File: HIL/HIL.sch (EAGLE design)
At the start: 245 parts, among them J1 JTAG_ARM_10PIN, J4 JTAG_ARM_10PIN, U1 CD74HC4067SM96, U10 INA219AIDCNR, U11 INA219AIDCNR, U12 INA219AIDCNR, U14 ADUM1201ARZ, U15 SN65HVD230D, U16 TL1963AKTTR., U17 FT230XS, U2 TL1963AKTTR., U3 CD74HC4067SM96, U4 CD74HC4067SM96, U5 MCP4725A0T-E/CH, U6 TL1963AKTTR., U7 MCP2003-E/SN, U8 TM4C1294NCPDT, U9 INA219AIDCNR, X1 A1944-50, X2 A1944-50, X4 A1944-50, Y3 NX3225GA

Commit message: smal fixes
better 3v3 plane coverage
add labels
fix tracks which are not straight or 45 degree
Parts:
- renumbered STANDOFF1 to STANDOFF3, STANDOFF5 to STANDOFF4
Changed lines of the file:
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@@
 <part name="U$5" library="SparkFun-DiscreteSemi" deviceset="MMBZ27VCLT1" device="" value="zener_3.3V"/>
 <part name="U$10" library="SparkFun-DiscreteSemi" deviceset="MMBZ27VCLT1" device="" value="zener_3.3V"/>
-<part name="STANDOFF1" library="SparkFun-Electromechanical" deviceset="STAND-OFF" device=""/>
+<part name="STANDOFF3" library="SparkFun-Electromechanical" deviceset="STAND-OFF" device=""/>
 <part name="STANDOFF2" library="SparkFun-Electromechanical" deviceset="STAND-OFF" device=""/>
-<part name="STANDOFF5" library="SparkFun-Electromechanical" deviceset="STAND-OFF" device=""/>
+<part name="STANDOFF4" library="SparkFun-Electromechanical" deviceset="STAND-OFF" device=""/>
 <part name="STANDOFF6" library="SparkFun-Electromechanical" deviceset="STAND-OFF" device=""/>
 <part name="R72" library="resistor" deviceset="R-EU_" device="R0402" value="4k7"/>
@@
 <instance part="S1" gate="1" x="27.94" y="127" rot="R270"/>
 <instance part="F1" gate="1" x="22.86" y="152.4" rot="R270"/>
-<instance part="STANDOFF1" gate="G$1" x="289.56" y="27.94"/>
+<instance part="STANDOFF3" gate="G$1" x="289.56" y="27.94"/>
 <instance part="STANDOFF2" gate="G$1" x="294.64" y="27.94"/>
-<instance part="STANDOFF5" gate="G$1" x="309.88" y="27.94"/>
+<instance part="STANDOFF4" gate="G$1" x="309.88" y="27.94"/>
 <instance part="STANDOFF6" gate="G$1" x="314.96" y="27.94"/>
 <instance part="R72" gate="G$1" x="154.94" y="195.58" rot="R180"/>

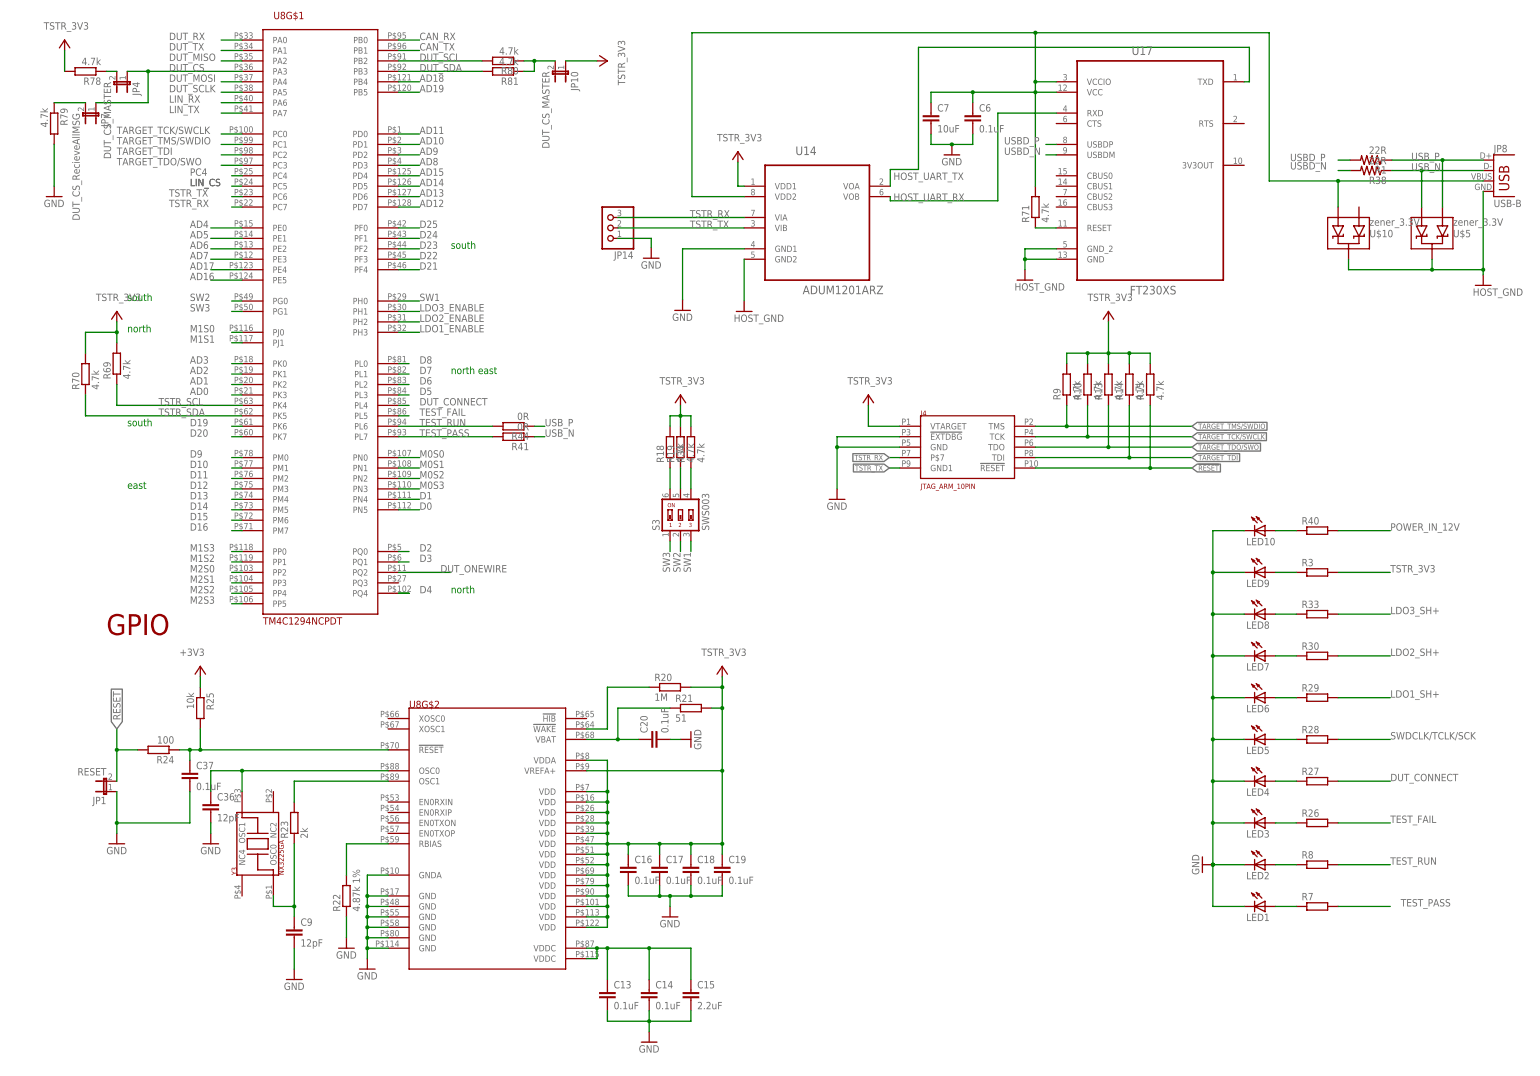
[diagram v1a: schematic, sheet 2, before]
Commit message: Change:  - MCU to a proper package Add:        - labels                 - i2c header                 - UART header
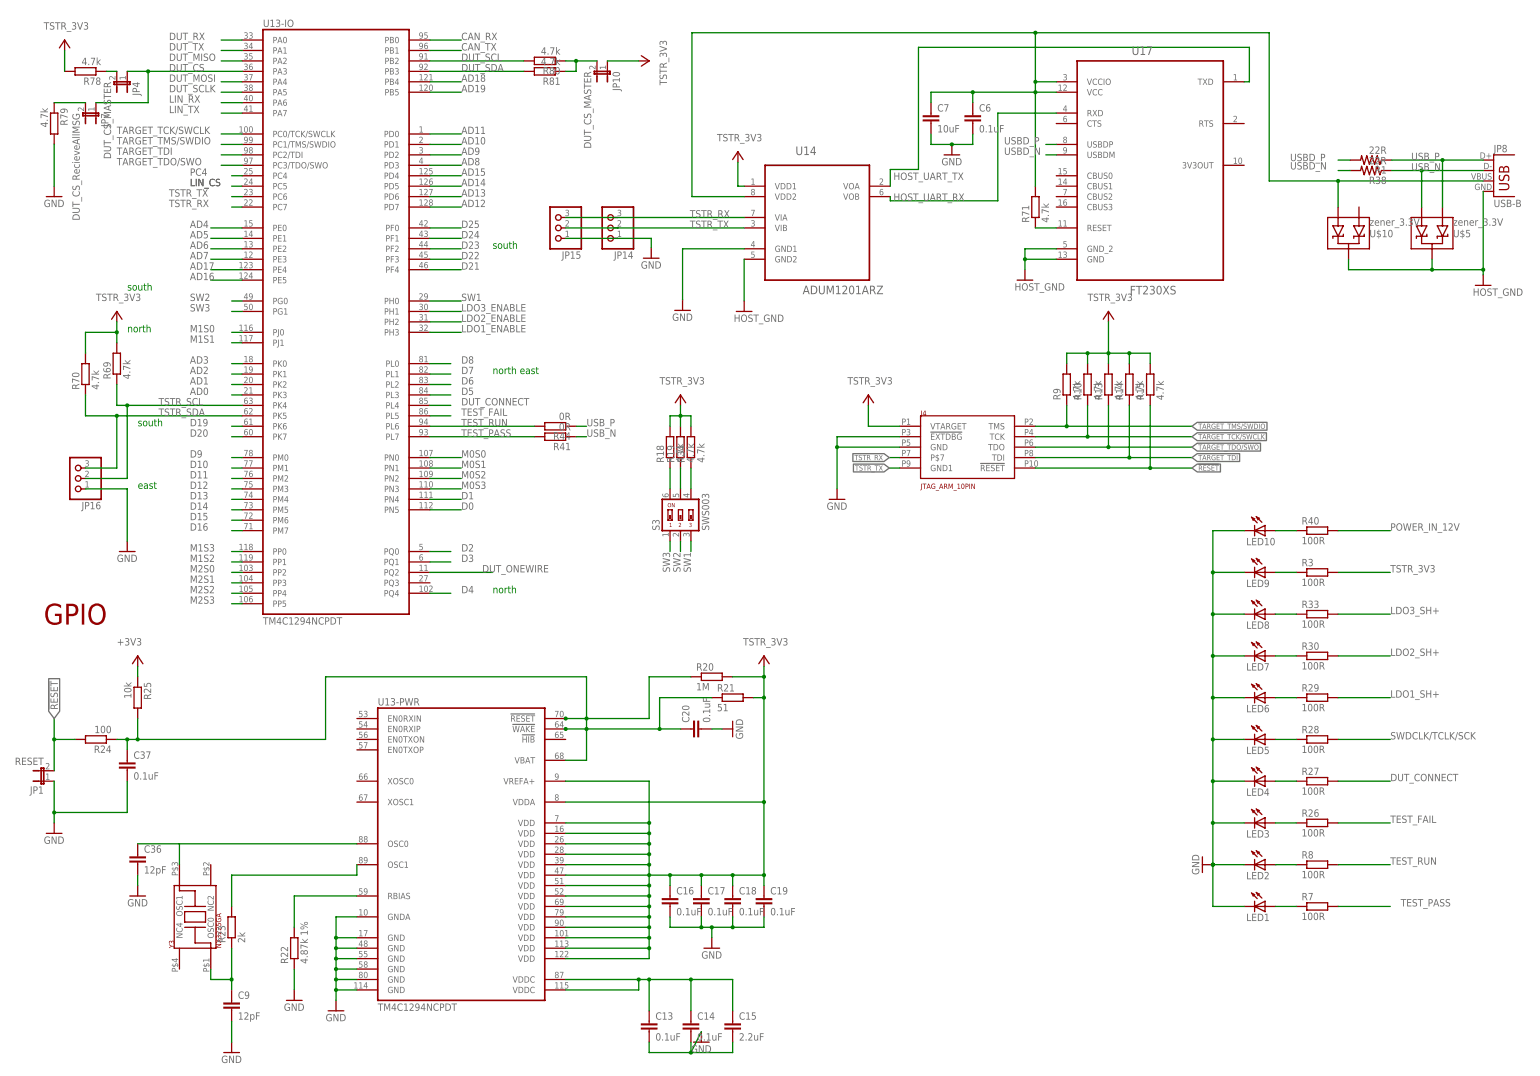
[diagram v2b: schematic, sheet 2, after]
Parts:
- removed U8: TM4C1294NCPDT, MRDT-Microcontrollers:TM4C1294NCPDT
- added JP15, JP16: (no value), JDT-1800_smahed:PINHD-1X3CB
- added U13: TM4C1294NCPDT, ti-tiva:TM4C1294NCPDT
- R26, R27, R28, R29, R3, R30, R33, R40, R7, R8: value (none) -> 100R
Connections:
- removed net N_$24: R20.1, U8G$2.!WAKE@64
- removed net N_$33: C37.1, R24.1, R25.2, U8G$2.!RESET@70
- net AD0: now also U13-IO.PK3@21; no longer U8G$1.PK3@21
- net AD1: now also U13-IO.PK2@20; no longer U8G$1.PK2@20
- net AD10: now also U13-IO.PD1@2; no longer U8G$1.PD1@2
- net AD11: now also U13-IO.PD0@1; no longer U8G$1.PD0@1
- net AD12: now also U13-IO.PD7@128; no longer U8G$1.PD7@128
- net AD13: now also U13-IO.PD6@127; no longer U8G$1.PD6@127
- net AD14: now also U13-IO.PD5@126; no longer U8G$1.PD5@126
- net AD15: now also U13-IO.PD4@125; no longer U8G$1.PD4@125
- net AD16: now also U13-IO.PE5@124; no longer U8G$1.PE5@124
- net AD17: now also U13-IO.PE4@123; no longer U8G$1.PE4@123
- net AD18: now also U13-IO.PB4@121; no longer U8G$1.PB4@121
- net AD19: now also U13-IO.PB5@120; no longer U8G$1.PB5@120
- net AD2: now also U13-IO.PK1@19; no longer U8G$1.PK1@19
- net AD3: now also U13-IO.PK0@18; no longer U8G$1.PK0@18
- net AD4: now also U13-IO.PE0@15; no longer U8G$1.PE0@15
- net AD5: now also U13-IO.PE1@14; no longer U8G$1.PE1@14
- net AD6: now also U13-IO.PE2@13; no longer U8G$1.PE2@13
- net AD7: now also U13-IO.PE3@12; no longer U8G$1.PE3@12
- net AD8: now also U13-IO.PD3@4; no longer U8G$1.PD3@4
- net AD9: now also U13-IO.PD2@3; no longer U8G$1.PD2@3
- net CAN_RX: now also U13-IO.PB0@95; no longer U8G$1.PB0@95
- net CAN_TX: now also U13-IO.PB1@96; no longer U8G$1.PB1@96
- net D0: now also U13-IO.PN5@112; no longer U8G$1.PN5@112
- net D1: now also U13-IO.PN4@111; no longer U8G$1.PN4@111
- net D10: now also U13-IO.PM1@77; no longer U8G$1.PM1@77
- net D11: now also U13-IO.PM2@76; no longer U8G$1.PM2@76
- net D12: now also U13-IO.PM3@75; no longer U8G$1.PM3@75
- net D13: now also U13-IO.PM4@74; no longer U8G$1.PM4@74
- net D14: now also U13-IO.PM5@73; no longer U8G$1.PM5@73
- net D15: now also U13-IO.PM6@72; no longer U8G$1.PM6@72
- net D16: now also U13-IO.PM7@71; no longer U8G$1.PM7@71
- net D19: now also U13-IO.PK6@61; no longer U8G$1.PK6@61
- net D2: now also U13-IO.PQ0@5; no longer U8G$1.PQ0@5
- net D20: now also U13-IO.PK7@60; no longer U8G$1.PK7@60
- net D21: now also U13-IO.PF4@46; no longer U8G$1.PF4@46
- net D22: now also U13-IO.PF3@45; no longer U8G$1.PF3@45
- net D23: now also U13-IO.PF2@44; no longer U8G$1.PF2@44
- net D24: now also U13-IO.PF1@43; no longer U8G$1.PF1@43
- net D25: now also U13-IO.PF0@42; no longer U8G$1.PF0@42
- net D3: now also U13-IO.PQ1@6; no longer U8G$1.PQ1@6
- net D4: now also U13-IO.PQ4@102; no longer U8G$1.PQ4@102
- net D5: now also U13-IO.PL3@84; no longer U8G$1.PL3@84
- net D6: now also U13-IO.PL2@83; no longer U8G$1.PL2@83
- net D7: now also U13-IO.PL1@82; no longer U8G$1.PL1@82
- net D8: now also U13-IO.PL0@81; no longer U8G$1.PL0@81
- net D9: now also U13-IO.PM0@78; no longer U8G$1.PM0@78
- net DUT_CONNECT: now also U13-IO.PL4@85; no longer U8G$1.PL4@85
- net DUT_CS: now also U13-IO.PA3@36; no longer U8G$1.PA3@36
- net DUT_MISO: now also U13-IO.PA2@35; no longer U8G$1.PA2@35
- net DUT_MOSI: now also U13-IO.PA4@37; no longer U8G$1.PA4@37
- net DUT_ONEWIRE: now also U13-IO.PQ2@11; no longer U8G$1.PQ2@11
- net DUT_RX: now also U13-IO.PA0@33; no longer U8G$1.PA0@33
- net DUT_SCL: now also U13-IO.PB2@91; no longer U8G$1.PB2@91
- net DUT_SCLK: now also U13-IO.PA5@38; no longer U8G$1.PA5@38
- net DUT_SDA: now also U13-IO.PB3@92; no longer U8G$1.PB3@92
- net DUT_TX: now also U13-IO.PA1@34; no longer U8G$1.PA1@34
- net GND: now also JP15.1, JP16.1, U13-PWR.GND@114, U13-PWR.GND@17, U13-PWR.GND@48, U13-PWR.GND@55, U13-PWR.GND@58, U13-PWR.GND@80, U13-PWR.GNDA@10; no longer U8G$2.GND@114, U8G$2.GND@17, U8G$2.GND@48, U8G$2.GND@55, U8G$2.GND@58, U8G$2.GND@80, U8G$2.GNDA@10
- net LDO1_ENABLE: now also U13-IO.PH3@32; no longer U8G$1.PH3@32
- net LDO2_ENABLE: now also U13-IO.PH2@31; no longer U8G$1.PH2@31
- net LDO3_ENABLE: now also U13-IO.PH1@30; no longer U8G$1.PH1@30
- net LIN_CS: now also U13-IO.PC5@24; no longer U8G$1.PC5@24
- net LIN_RX: now also U13-IO.PA6@40; no longer U8G$1.PA6@40
- net LIN_TX: now also U13-IO.PA7@41; no longer U8G$1.PA7@41
- net M0S0: now also U13-IO.PN0@107; no longer U8G$1.PN0@107
- net M0S1: now also U13-IO.PN1@108; no longer U8G$1.PN1@108
- net M0S2: now also U13-IO.PN2@109; no longer U8G$1.PN2@109
- net M0S3: now also U13-IO.PN3@110; no longer U8G$1.PN3@110
- net M1S0: now also U13-IO.PJ0@116; no longer U8G$1.PJ0@116
- net M1S1: now also U13-IO.PJ1@117; no longer U8G$1.PJ1@117
- net M1S2: now also U13-IO.PP1@119; no longer U8G$1.PP1@119
- net M1S3: now also U13-IO.PP0@118; no longer U8G$1.PP0@118
- net M2S0: now also U13-IO.PP2@103; no longer U8G$1.PP2@103
- net M2S1: now also U13-IO.PP3@104; no longer U8G$1.PP3@104
- net M2S2: now also U13-IO.PP4@105; no longer U8G$1.PP4@105
- net M2S3: now also U13-IO.PP5@106; no longer U8G$1.PP5@106
- net N_$2: now also C37.1, R20.1, R24.1, R25.2, U13-PWR.!RESET@70, U13-PWR.!WAKE@64, U13-PWR.VBAT@68; no longer U8G$2.VBAT@68
- net N_$28: now also U13-PWR.VDDC@115, U13-PWR.VDDC@87; no longer U8G$2.VDDC@115, U8G$2.VDDC@87
- net N_$29: now also U13-PWR.RBIAS@59; no longer U8G$2.RBIAS@59
- net N_$30: now also U13-PWR.OSC1@89; no longer U8G$2.OSC1@89
- net N_$31: now also U13-PWR.OSC0@88; no longer U8G$2.OSC0@88
- net PC4: now also U13-IO.PC4@25; no longer U8G$1.PC4@25
- net SW1: now also U13-IO.PH0@29; no longer U8G$1.PH0@29
- net SW2: now also U13-IO.PG0@49; no longer U8G$1.PG0@49
- net SW3: now also U13-IO.PG1@50; no longer U8G$1.PG1@50
- net TARGET_TCK/SWCLK: now also U13-IO.PC0/TCK/SWCLK@100; no longer U8G$1.PC0@100
- net TARGET_TDI: now also U13-IO.PC2/TDI@98; no longer U8G$1.PC2@98
- net TARGET_TDO/SWO: now also U13-IO.PC3/TDO/SWO@97; no longer U8G$1.PC3@97
- net TARGET_TMS/SWDIO: now also U13-IO.PC1/TMS/SWDIO@99; no longer U8G$1.PC1@99
- net TEST_FAIL: now also U13-IO.PL5@86; no longer U8G$1.PL5@86
- net TEST_PASS: now also U13-IO.PL7@93; no longer U8G$1.PL7@93
- net TEST_RUN: now also U13-IO.PL6@94; no longer U8G$1.PL6@94
- net TSTR_3V3: now also U13-PWR.VDD@101, U13-PWR.VDD@113, U13-PWR.VDD@122, U13-PWR.VDD@16, U13-PWR.VDD@26, U13-PWR.VDD@28, U13-PWR.VDD@39, U13-PWR.VDD@47, U13-PWR.VDD@51, U13-PWR.VDD@52, U13-PWR.VDD@69, U13-PWR.VDD@7, U13-PWR.VDD@79, U13-PWR.VDD@90, U13-PWR.VDDA@8, U13-PWR.VREFA+@9; no longer U8G$2.VDD@101, U8G$2.VDD@113, U8G$2.VDD@122, U8G$2.VDD@16, U8G$2.VDD@26, U8G$2.VDD@28, U8G$2.VDD@39, U8G$2.VDD@47, U8G$2.VDD@51, U8G$2.VDD@52, U8G$2.VDD@69, U8G$2.VDD@7, U8G$2.VDD@79, U8G$2.VDD@90, U8G$2.VDDA@8, U8G$2.VREFA+@9
- net TSTR_RX: now also JP15.3, U13-IO.PC7@22; no longer U8G$1.PC7@22
- net TSTR_SCL: now also JP16.2, U13-IO.PK4@63; no longer U8G$1.PK4@63
- net TSTR_SDA: now also JP16.3, U13-IO.PK5@62; no longer U8G$1.PK5@62
- net TSTR_TX: now also JP15.2, U13-IO.PC6@23; no longer U8G$1.PC6@23
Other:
- moved on the sheet: C13, C14, C15, C16, C17, C18, C19, C20, C36, C37, C9, JP1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
